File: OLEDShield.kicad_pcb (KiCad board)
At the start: 2 copper layers, 68.6 x 53.3 mm, 257 parts, among them P1 CONN_5X2, P2 CONN_5X2, P3 CONN_1, P4 CONN_1, P5 CONN_1, SW1 SW_PUSHBUTTON

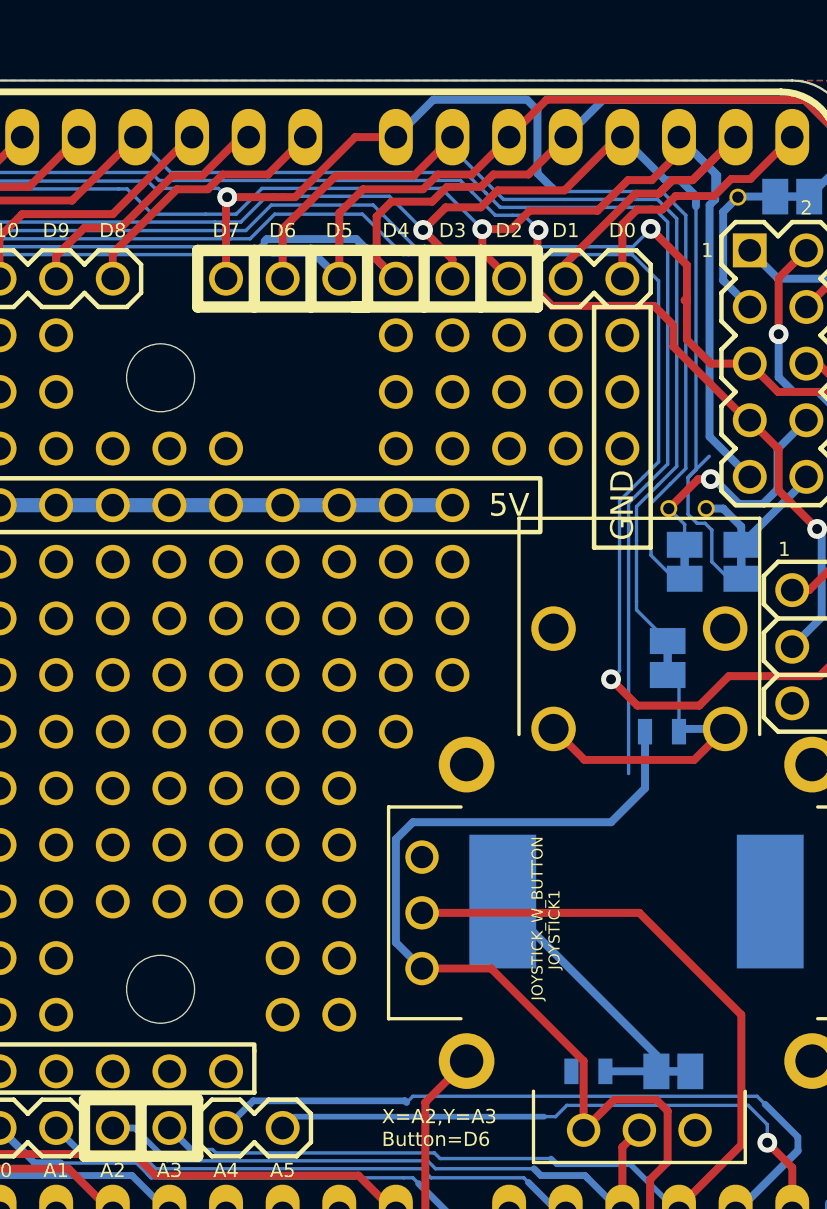
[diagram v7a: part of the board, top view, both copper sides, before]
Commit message: Move piezo from D11 to D9
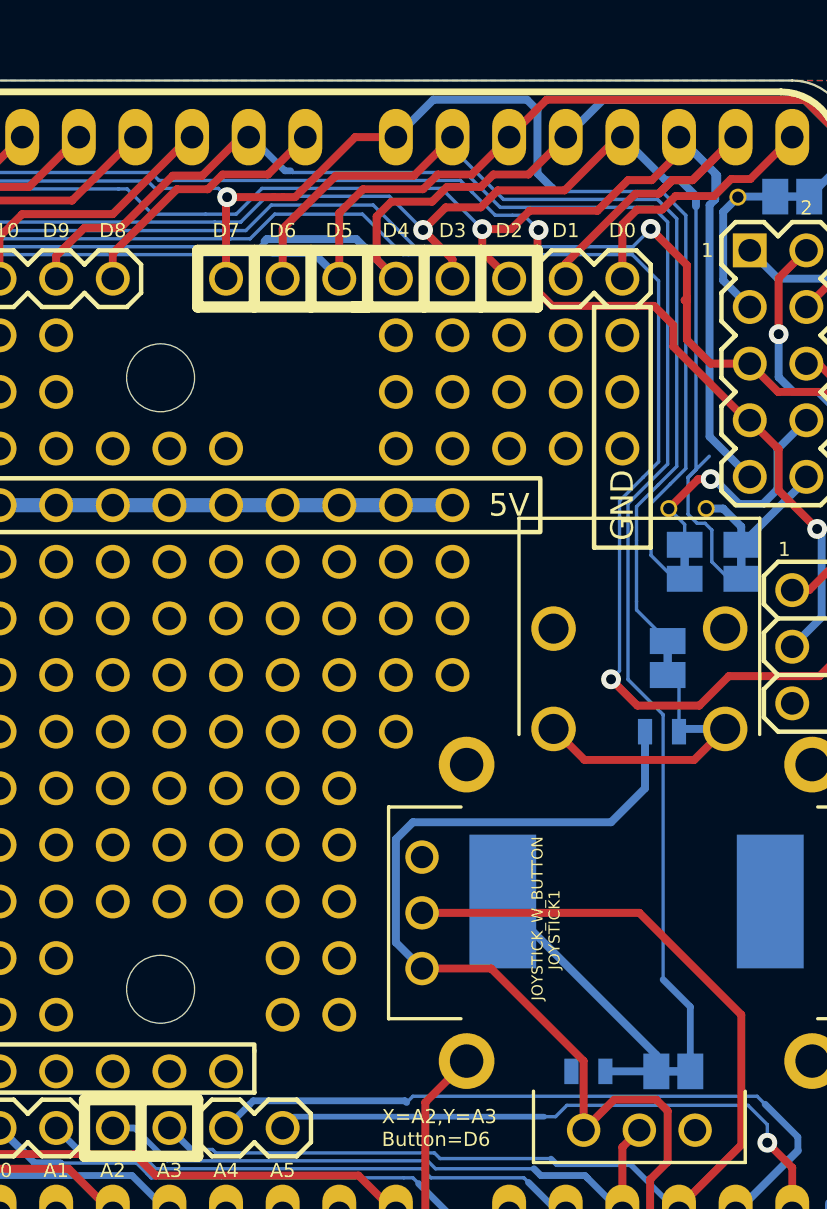
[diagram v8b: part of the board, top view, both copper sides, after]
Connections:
- SJ1 pad 1: /D11 -> /D9
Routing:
- net /D9: track 11.9 -> 72.2 mm
- net /D11: track 63.3 -> 12.4 mm
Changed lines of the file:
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@@
   (general
     (links 115)
-    (no_connects 1)
-    (area 216.391067 218.5924 288.290001 277.3132)
+    (no_connects 0)
+    (area 218.389999 223.469999 287.070001 276.910001)
     (thickness 1.6)
     (drawings 580)
@@
   )
   (setup
-    (last_trace_width 0.3556)
+    (last_trace_width 0.3048)
     (user_trace_width 0.1524)
     (user_trace_width 0.2032)
@@
     (pad 1 smd rect (at -0.762 0 180) (size 1.1684 1.6002)
       (layers B.Cu B.Mask)
-      (net 13 /D11)
+      (net 18 /D9)
     )
     (pad 2 smd rect (at 0.762 0 180) (size 1.1684 1.6002)
@@
   (segment (start 243.84 230.4288) (end 245.364 228.9048) (width 0.3556) (layer F.Cu) (net 13))
   (segment (start 245.364 228.9048) (end 249.6312 228.9048) (width 0.3556) (layer F.Cu) (net 13))
-  (segment (start 274.8534 229.209602) (end 275.59 229.209602) (width 0.1524) (layer B.Cu) (net 13))
   (segment (start 249.6312 228.9048) (end 252.476 226.06) (width 0.3556) (layer F.Cu) (net 13))
-  (segment (start 274.8534 229.209602) (end 274.32 229.209602) (width 0.1524) (layer B.Cu) (net 13))
-  (segment (start 252.476 226.06) (end 254.0635 227.6475) (width 0.1524) (layer B.Cu) (net 13))
-  (segment (start 268.859 229.209602) (end 274.32 229.209602) (width 0.1524) (layer B.Cu) (net 13))
-  (segment (start 268.194801 228.570801) (end 268.833602 229.209602) (width 0.1524) (layer B.Cu) (net 13))
-  (segment (start 268.833602 229.209602) (end 268.859 229.209602) (width 0.1524) (layer B.Cu) (net 13))
-  (segment (start 254.0635 227.6475) (end 267.276602 227.6475) (width 0.1524) (layer B.Cu) (net 13))
-  (segment (start 267.276602 227.6475) (end 268.194801 228.565699) (width 0.1524) (layer B.Cu) (net 13))
-  (segment (start 268.194801 228.565699) (end 268.194801 228.570801) (width 0.1524) (layer B.Cu) (net 13))
-  (segment (start 275.59 229.209602) (end 275.691602 229.209602) (width 0.1524) (layer B.Cu) (net 13))
-  (segment (start 275.691602 229.209602) (end 276.352 229.87) (width 0.1524) (layer B.Cu) (net 13))
-  (segment (start 276.352 229.87) (end 276.352 240.723398) (width 0.1524) (layer B.Cu) (net 13))
-  (segment (start 276.352 240.723398) (end 275.428699 241.646699) (width 0.1524) (layer B.Cu) (net 13))
-  (segment (start 274.599398 243.6495) (end 274.599398 242.476) (width 0.1524) (layer B.Cu) (net 13))
-  (segment (start 274.599398 242.476) (end 275.428699 241.646699) (width 0.1524) (layer B.Cu) (net 13))
-  (segment (start 274.599398 243.6495) (end 274.599398 254.609602) (width 0.1524) (layer B.Cu) (net 13))
   (segment (start 241.3 232.41) (end 241.9096 232.41) (width 0.3556) (layer F.Cu) (net 14))
   (segment (start 241.9096 232.41) (end 243.2304 231.0892) (width 0.3556) (layer F.Cu) (net 14))
@@
   (segment (start 254.333066 228.3968) (end 255.7272 228.3968) (width 0.3556) (layer F.Cu) (net 17))
   (segment (start 251.46 231.269866) (end 254.333066 228.3968) (width 0.3556) (layer F.Cu) (net 17))
+  (segment (start 259.4356 227.5713) (end 259.5118 227.6475) (width 0.1524) (layer B.Cu) (net 18))
+  (segment (start 259.181602 227.5713) (end 259.4356 227.5713) (width 0.3048) (layer B.Cu) (net 18))
+  (segment (start 257.556 226.06) (end 257.670302 226.06) (width 0.3048) (layer B.Cu) (net 18) (status C00000))
+  (segment (start 257.670302 226.06) (end 258.826 227.215698) (width 0.3048) (layer B.Cu) (net 18) (status 400000))
+  (segment (start 258.826 227.215698) (end 259.181602 227.5713) (width 0.3048) (layer B.Cu) (net 18))
+  (segment (start 277.368 265.0744) (end 277.368 267.97) (width 0.3048) (layer B.Cu) (net 18) (status 800000))
+  (segment (start 276.1488 263.8552) (end 277.368 265.0744) (width 0.3048) (layer B.Cu) (net 18))
+  (segment (start 276.1488 251.968) (end 276.1488 263.8552) (width 0.1524) (layer B.Cu) (net 18))
+  (segment (start 274.574 250.3932) (end 276.1488 251.968) (width 0.1524) (layer B.Cu) (net 18))
+  (segment (start 274.574 242.501398) (end 274.574 250.3932) (width 0.1524) (layer B.Cu) (net 18))
+  (segment (start 276.352 240.723398) (end 274.574 242.501398) (width 0.1524) (layer B.Cu) (net 18))
+  (segment (start 276.352 229.87) (end 276.352 240.723398) (width 0.1524) (layer B.Cu) (net 18))
+  (segment (start 275.691602 229.209602) (end 276.352 229.87) (width 0.1524) (layer B.Cu) (net 18))
+  (segment (start 268.838704 229.209602) (end 275.691602 229.209602) (width 0.1524) (layer B.Cu) (net 18))
+  (segment (start 267.276602 227.6475) (end 268.838704 229.209602) (width 0.1524) (layer B.Cu) (net 18))
+  (segment (start 259.5118 227.6475) (end 267.276602 227.6475) (width 0.1524) (layer B.Cu) (net 18))
   (segment (start 248.92 232.41) (end 248.92 231.394002) (width 0.3556) (layer F.Cu) (net 18))
   (segment (start 257.2004 226.06) (end 257.556 226.06) (width 0.3556) (layer F.Cu) (net 18))
